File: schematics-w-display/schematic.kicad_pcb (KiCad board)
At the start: 2 copper layers, 59.8 x 61.5 mm, 12 parts, among them J1 Conn_01x21_Female_ESP, J2 Conn_01x06_Female_BME280, J3 Conn_01x21_Female_ESP, J4 Conn_01x08_Female_Display, SW1 Bootloader_Push, SW2 RST_Push

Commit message: Move boot button up
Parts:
- moved SW1 12.7 mm to (138.3, 63.7), turned to 0 degrees
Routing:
- net Net-(J3-Pad20): track 48.0 -> 33.4 mm
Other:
- outline, holes or cut-outs redrawn

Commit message: Add additional cable hole
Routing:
- net Net-(J3-Pad20): track 33.4 -> 39.9 mm
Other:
- outline, holes or cut-outs redrawn
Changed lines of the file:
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@@
   (general
     (thickness 1.6)
-    (drawings 17)
-    (tracks 84)
+    (drawings 22)
+    (tracks 85)
     (zones 0)
     (modules 12)
@@
     )
   )
+  (gr_line (start 142.1 108.8) (end 142.1 104.3) (layer Edge.Cuts) (width 0.05))
+  (gr_line (start 142.1 104.3) (end 146.9 104.3) (layer Edge.Cuts) (width 0.05))
+  (gr_line (start 146.9 104.3) (end 146.9 74.1) (layer Edge.Cuts) (width 0.05))
+  (gr_line (start 146.9 108.8) (end 146.9 108.8) (layer Edge.Cuts) (width 0.05))
+  (gr_line (start 146.9 108.8) (end 142.1 108.8) (layer Edge.Cuts) (width 0.05))
   (gr_text "USB CONN" (at 122.4 121.8) (layer F.SilkS)
     (effects (font (size 1 1) (thickness 0.15)))
@@
   (gr_line (start 146.9 61.6) (end 87.1 61.6) (layer Edge.Cuts) (width 0.05))
   (gr_line (start 87.1 61.6) (end 87.1 123.063) (layer Edge.Cuts) (width 0.05))
-  (gr_line (start 146.9 123.079) (end 146.9 74.1) (layer Edge.Cuts) (width 0.05))
+  (gr_line (start 146.9 123.079) (end 146.9 108.8) (layer Edge.Cuts) (width 0.05))
   (segment (start 107.425 75.525) (end 110 75.525) (width 0.75) (layer B.Cu) (net 1))
   (segment (start 104.88 72.98) (end 107.425 75.525) (width 0.75) (layer B.Cu) (net 1))
@@
   (segment (start 118.115 72.985) (end 126.7 64.4) (width 0.5) (layer B.Cu) (net 32))
   (segment (start 110 72.985) (end 118.115 72.985) (width 0.5) (layer B.Cu) (net 32))
+  (segment (start 138.3 68.2) (end 144.8 68.2) (width 0.5) (layer B.Cu) (net 32))
   (segment (start 89.7 86.8) (end 89.45 86.8) (width 0.75) (layer B.Cu) (net 33))
   (segment (start 93.1 86.74) (end 95.04 86.74) (width 0.75) (layer B.Cu) (net 33))
@@
     (polygon
       (pts
-        (xy 146.4 69.7) (xy 142.3 69.7) (xy 142.3 74.7) (xy 146.4 74.7) (xy 146.4 122.5)
-        (xy 87.7 122.5) (xy 87.6 62.1) (xy 146.4 62.1)
+        (xy 146.4 69.7) (xy 142.3 69.7) (xy 142.3 74.7) (xy 146.4 74.7) (xy 146.4 103.8)
+        (xy 141.6 103.8) (xy 141.6 109.3) (xy 146.4 109.3) (xy 146.4 122.5) (xy 87.7 122.5)
+        (xy 87.6 62.1) (xy 146.4 62.1)
       )
     )
@@
       (pts
         (xy 146.4 69.7) (xy 142.3 69.7) (xy 142.3 70.6) (xy 142.3 74.7) (xy 146.4 74.7)
-        (xy 146.4 122.5) (xy 87.6 122.5) (xy 87.6 62.1) (xy 146.4 62.1)
+        (xy 146.4 103.8) (xy 141.6 103.8) (xy 141.6 109.3) (xy 146.4 109.3) (xy 146.4 122.5)
+        (xy 87.6 122.5) (xy 87.6 62.1) (xy 146.4 62.1)
       )
     )

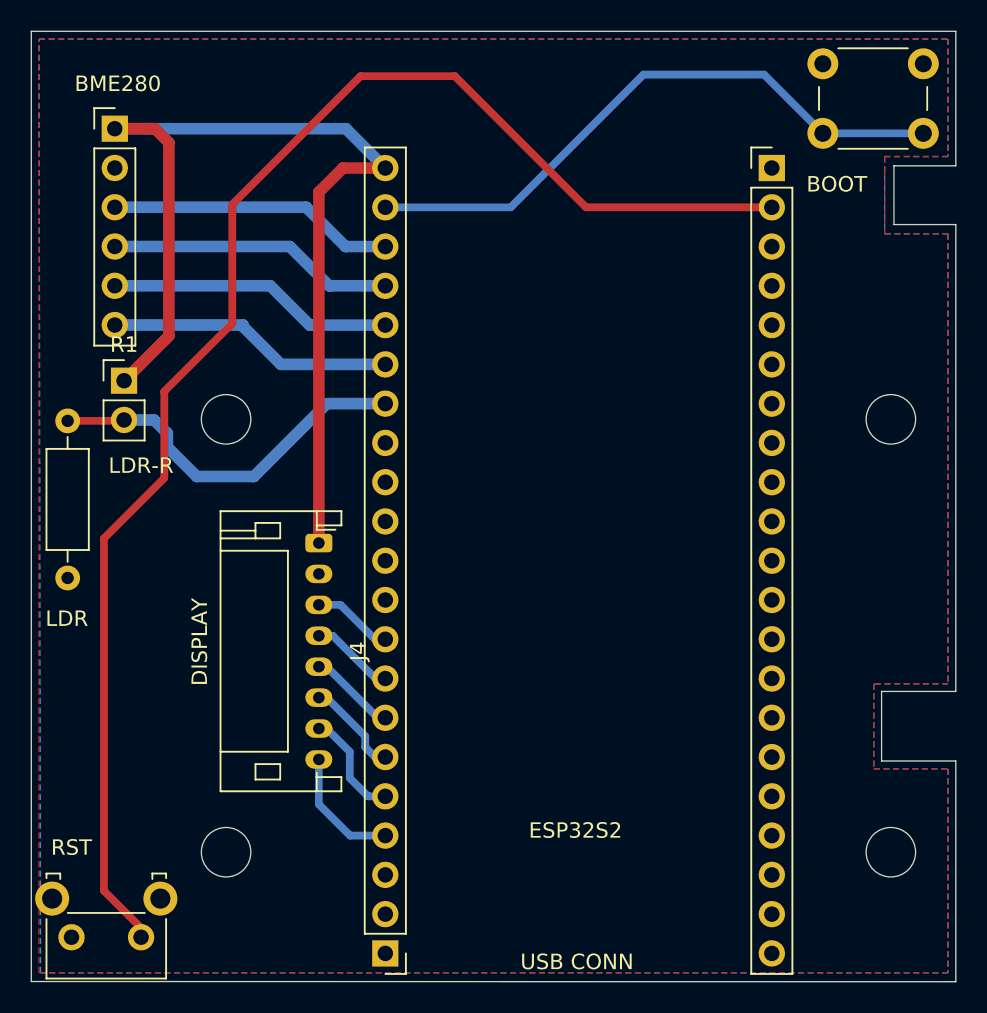
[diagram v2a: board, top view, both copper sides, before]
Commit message: Remove LDR, add serial converter
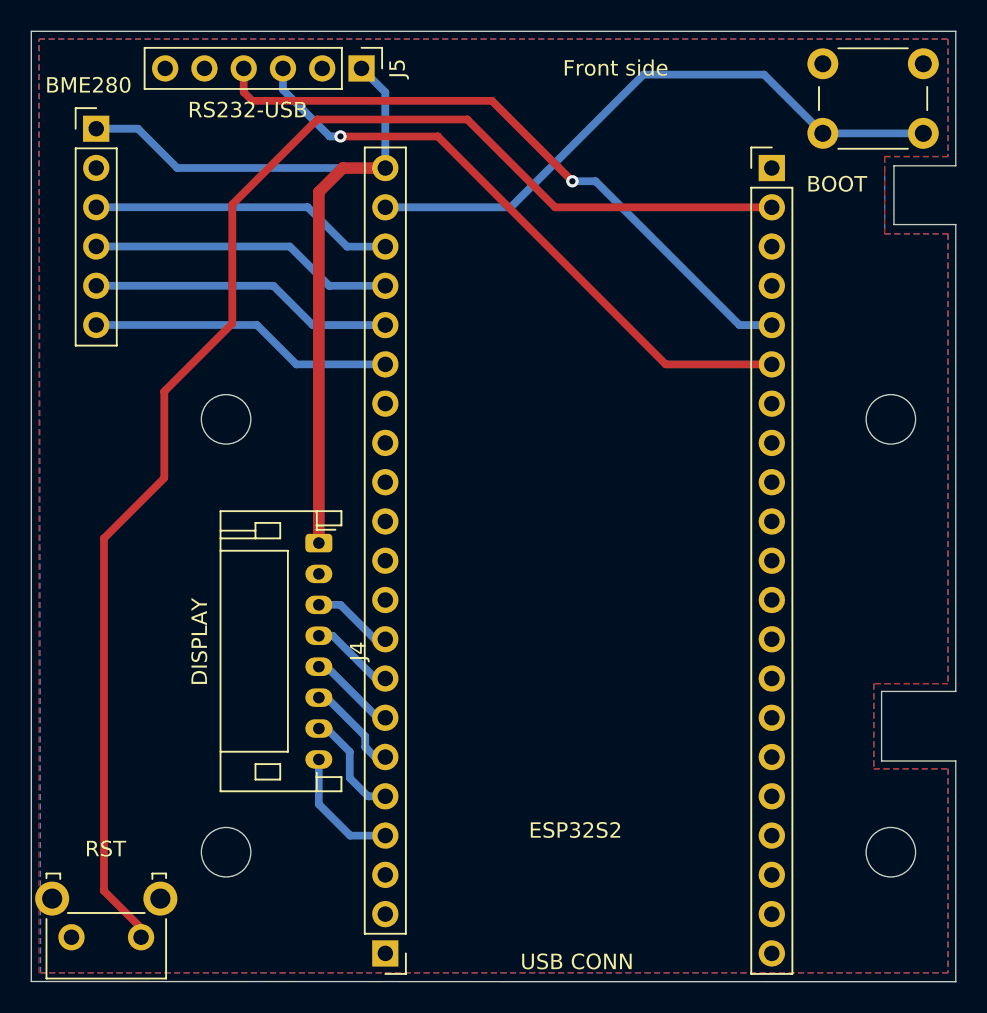
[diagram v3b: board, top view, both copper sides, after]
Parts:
- removed R1: LDR03, Connector_PinHeader_2.54mm:PinHeader_1x02_P2.54mm_Vertical
- removed R2: 10kOhm, Resistor_THT:R_Axial_DIN0207_L6.3mm_D2.5mm_P10.16mm_Horizontal
- added J5: Conn_01x06_Female_RS232_USB, Connector_PinHeader_2.54mm:PinHeader_1x06_P2.54mm_Vertical, F.Cu at (108.5, 64.0)
- moved J2 1.20 mm to (91.3, 67.9)
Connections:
- J1 pad 5: Net-(J1-Pad5) -> /RX-TX
- J1 pad 6: Net-(J1-Pad6) -> /TX-RX
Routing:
- net /RX-TX: track 0.00 -> 41.9 mm, vias 0 -> 1
- net /TX-RX: track 0.00 -> 40.4 mm, vias 0 -> 1
- net Net-(J3-Pad15): track 24.8 -> 0.00 mm
- net 3v3: track 67.0 -> 54.6 mm
- net Net-(J1-Pad2): track 93.9 -> 91.6 mm
- net /SDO: track 18.6 -> 19.8 mm
- net /SDA: track 18.6 -> 19.8 mm
- net /CSB: track 18.6 -> 19.8 mm
- net /SCL: track 18.6 -> 19.8 mm
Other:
- board text added: "Back side"
- board text added: "Front side"
- board text added: "RS232-USB"
- board text removed: "LDR"
- board text removed: "LDR-R"
